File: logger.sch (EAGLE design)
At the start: 131 parts, among them IC1 LTC4412, IC2 ATMEGA8, IC3 FT232RL, IC4 ATMEGA8, IC5 FT232RL, J1 POWER_JACKPTH, Q1 FDN360P, Q2 FDN360P, Q3 16MHz, Q4 16MHz, Q5 2N7002PW, U1 FT232RL, U2 FT232RLSSOP, U3 FT231XS, X5 USB-MICROB

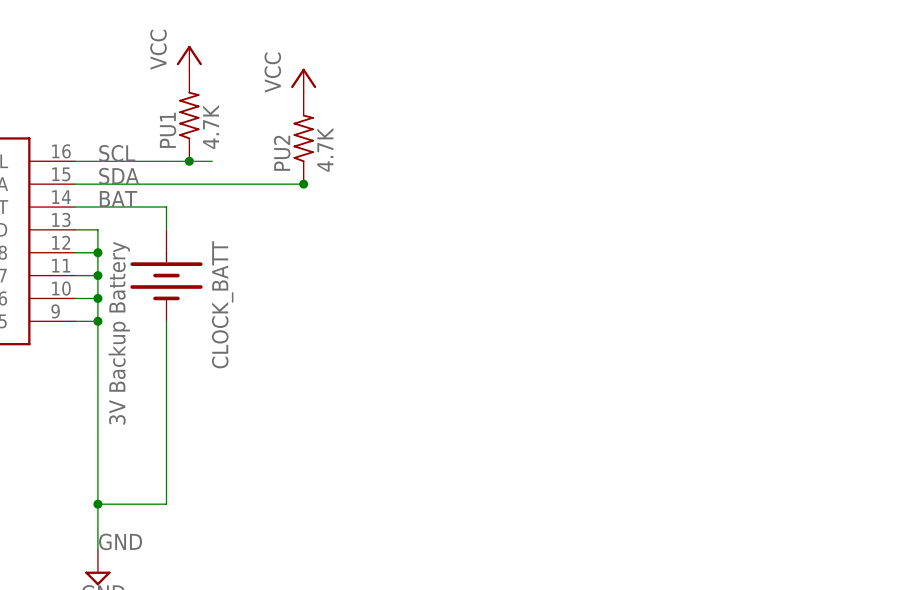
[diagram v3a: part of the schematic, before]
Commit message: Added diode OR, not connected yet
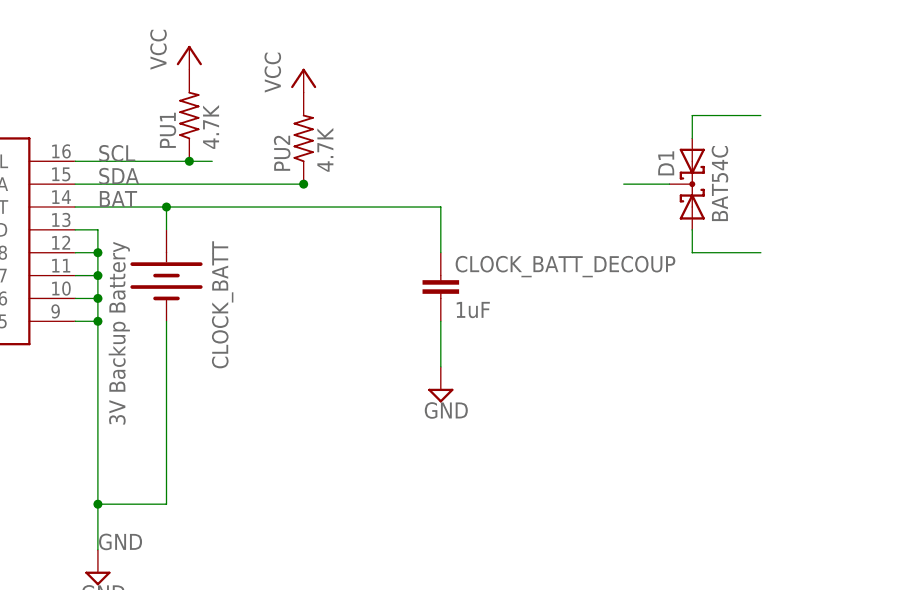
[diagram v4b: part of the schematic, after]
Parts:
- added CLOCK_BATT_DECOUP: 1uF, rcl:C-EUC0603
- added D1: BAT54C, diode:BAT54C
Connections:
- new net N$66: D1.A1
- new net N$67: D1.A2
- new net N$68: D1.CC
- net BAT: now also CLOCK_BATT_DECOUP.1
- net GND: now also CLOCK_BATT_DECOUP.2
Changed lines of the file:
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@@
 <setting verticaltext="up"/>
 </settings>
-<grid distance="0.1" unitdist="inch" unit="inch" style="lines" multiple="1" display="yes" altdistance="0.01" altunitdist="inch" altunit="inch"/>
+<grid distance="0.1" unitdist="inch" unit="inch" style="lines" multiple="1" display="no" altdistance="0.01" altunitdist="inch" altunit="inch"/>
 <layers>
 <layer number="1" name="Top" color="4" fill="1" visible="no" active="no"/>
@@
 <part name="SUPPLY46" library="supply2" deviceset="GND" device=""/>
 <part name="U$9" library="MyPOW" deviceset="VUSB" device=""/>
+<part name="CLOCK_BATT_DECOUP" library="rcl" deviceset="C-EU" device="C0603" value="1uF"/>
+<part name="SUPPLY47" library="supply2" deviceset="GND" device=""/>
+<part name="D1" library="diode" deviceset="BAT54C" device=""/>
 </parts>
 <sheets>
@@
 <instance part="SUPPLY46" gate="GND" x="-91.44" y="-154.94"/>
 <instance part="U$9" gate="G$1" x="17.78" y="-111.76"/>
+<instance part="CLOCK_BATT_DECOUP" gate="G$1" x="312.42" y="208.28"/>
+<instance part="SUPPLY47" gate="GND" x="312.42" y="195.58"/>
+<instance part="D1" gate="G$1" x="340.36" y="218.44" rot="R90"/>
 </instances>
 <busses>
@@
 <pinref part="SUPPLY46" gate="GND" pin="GND"/>
 </segment>
+<segment>
+<pinref part="CLOCK_BATT_DECOUP" gate="G$1" pin="2"/>
+<pinref part="SUPPLY47" gate="GND" pin="GND"/>
+<wire x1="312.42" y1="198.12" x2="312.42" y2="203.2" width="0.1524" layer="91"/>
+</segment>
 </net>
 <net name="TX-O" class="0">
@@
 <pinref part="CLOCK_BATT" gate="G$1" pin="+"/>
 <pinref part="RTC" gate="G$1" pin="VBAT"/>
+<wire x1="281.94" y1="215.9" x2="312.42" y2="215.9" width="0.1524" layer="91"/>
+<junction x="281.94" y="215.9"/>
+<wire x1="312.42" y1="215.9" x2="312.42" y2="210.82" width="0.1524" layer="91"/>
+<pinref part="CLOCK_BATT_DECOUP" gate="G$1" pin="1"/>
 </segment>
 </net>
@@
 </segment>
 </net>
+<net name="N$66" class="0">
+<segment>
+<pinref part="D1" gate="G$1" pin="A1"/>
+<wire x1="340.36" y1="213.36" x2="340.36" y2="210.82" width="0.1524" layer="91"/>
+<wire x1="340.36" y1="210.82" x2="347.98" y2="210.82" width="0.1524" layer="91"/>
+</segment>
+</net>
+<net name="N$67" class="0">
+<segment>
+<pinref part="D1" gate="G$1" pin="A2"/>
+<wire x1="340.36" y1="223.52" x2="340.36" y2="226.06" width="0.1524" layer="91"/>
+<wire x1="340.36" y1="226.06" x2="347.98" y2="226.06" width="0.1524" layer="91"/>
+</segment>
+</net>
+<net name="N$68" class="0">
+<segment>
+<pinref part="D1" gate="G$1" pin="CC"/>
+<wire x1="337.82" y1="218.44" x2="332.74" y2="218.44" width="0.1524" layer="91"/>
+</segment>
+</net>

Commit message: New FTDI chip, power-saving clock circuits (h/t Gerhard), with Chad Sandell
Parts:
- removed C1, C10, C11, C12, C13, C16, C4, C5, C8, C9: 100n, rcl:C-EU
- removed C2, C3, C6, C7: 22p, rcl:C-EU
- removed C_RESET, USBD0, USBD2, USBD4: 0.1uF, resistor:C-EUC0603
- removed F1, F2: 500mA, rcl:L-EUL1812
- removed IC2, IC4: ATMEGA8, atmel:AT90S4433P
- removed IC3, IC5: FT232RL, SmartPrj:FT232RL
- removed J2, J3, J5, J6: (no value), pinhead:PINHD-1X8
- removed J4, J7: (no value), pinhead:PINHD-1X6
- removed JP7, JP8: USB-B, SparkFun-Connectors:USBPTH
- removed Q3, Q4: 16MHz, crystal:CRYTALHC49S
- removed R1, R3, R4, R5, R6, R7, R8, R9: 1k, rcl:R-EU_
- removed R10, R2: 100_NM, rcl:R-EU_
- removed R16: 10k, SparkFun-Passives:RESISTOR0402-RES
- removed RX, TX: (no value), SparkFun-LED:LED0603
- removed RX1, RX2, TX1, TX2: (no value), led:LED0805ROUND
- removed RX_SW: 1Kohm, rcl:R-US_R0603
- removed R_RXLED, R_TXLED, TX_SW: 1K, rcl:R-US_R0603
- removed SJ1: (no value), SparkFun-Passives:SOLDERJUMPER_2WAYS
- removed SJ2: TXLED, SparkFun-Passives:SOLDERJUMPERTRACE
- removed SJ3: RXLED, SparkFun-Passives:SOLDERJUMPERTRACE
- removed U1: FT232RL, SparkFun-DigitalIC:FT232RL-BASICSSOP
- removed U2: FT232RLSSOP, SparkFun-DigitalIC:FT232RLSSOP
- removed USBD1, USBD3, USBD5: 10uF, SparkFun:CAP_POL1206
- removed X1, X3: (no value), jumper:JP4E
- removed X2, X4: (no value), SmartPrj:PN61729
- removed X5: USB-MICROB, SparkFun-Connectors:USB-MICROB
- added PU3, PU4: 3K, rcl:R-US_R0603
- added RCKL1, RCLK2: 220ohm, rcl:R-US_R0603
- added RX_SW1: 1Kohm, rcl:R-US_R0603
- added TX_SW1: 1K, rcl:R-US_R0603
- added U$3, U$4: BSS138, SteveMarple:BSS138SOT23-3-HAND
- PU1, PU2: value 4.7K -> 3K
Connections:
- removed net +5V: C1.1, C10.1, C12.1, C5.1, IC2.AVCC, IC2.VCC, IC3.RESET#, IC3.VCC5I, IC3.VCCIO, IC4.AVCC, IC4.VCC, IC5.RESET#, IC5.VCC5I, IC5.VCCIO, R1.2, R3.2, R4.2, R5.2
- removed net AREF: IC2.AREF, IC4.AREF
- removed net CBUS0: U3.CBUS0
- removed net CBUS3: U3.CBUS3
- removed net CTS: IC3.CTS#, IC5.CTS#, U3.!CTS, X1.1, X3.1
- removed net D+: IC3.USBDP, IC5.USBDP, X2.3, X4.3
- removed net D-: IC3.USBDM, IC5.USBDM, X2.2, X4.2
- removed net M8RXD: IC3.TXD, IC5.TXD, R6.2, R8.2
- removed net M8TXD: IC3.RXD, IC5.RXD, R7.2, R9.2
- removed net MISO: IC2.(MISO)PB4, IC4.(MISO)PB4, J3.5, J6.5
- removed net MOSI: IC2.(MOSI)PB3, IC4.(MOSI)PB3, J3.4, J6.4
- removed net N$10: TX_SW.1, U1.RXD
- removed net N$11: C2.2, IC2.XTAL1, Q3.1
- removed net N$12: C3.2, IC2.XTAL2, Q3.2
- removed net N$13: IC2.(INT0)PD2, J2.3
- removed net N$14: IC2.(INT1)PD3, J2.4
- removed net N$15: IC2.(T0)PD4, J2.5
- removed net N$16: IC2.(T1)PD5, J2.6
- removed net N$17: IC2.(AIN0)PD6, J2.7
- removed net N$18: IC2.(AIN1)PD7, J2.8
- removed net N$19: IC2.(ADC0)PC0), J4.1
- removed net N$20: IC2.(ADC1)PC1, J4.2
- removed net N$21: IC2.(ADC2)PC2, J4.3
- removed net N$22: IC2.(ADC3)PC3, J4.4
- removed net N$23: IC2.(ADC4)PC4, J4.5
- removed net N$24: IC2.(ADC5)PC5, J4.6
- removed net N$25: IC2.(ICP)PB0, J3.1
- removed net N$26: IC2.(OC1)PB1, J3.2
- removed net N$28: F1.2, X4.1
- removed net N$3: JP5.D-, U1.USBDM
- removed net N$30: IC4.(INT0)PD2, J5.3
- removed net N$31: IC4.(INT1)PD3, J5.4
- removed net N$32: IC3.GPIO1, RX1.C
- removed net N$33: IC4.(T0)PD4, J5.5
- removed net N$34: IC3.GPIO0, TX1.C
- removed net N$35: R4.1, RX1.A
- removed net N$36: R5.1, TX1.A
- removed net N$37: IC4.(T1)PD5, J5.6
- removed net N$38: IC4.(AIN0)PD6, J5.7
- removed net N$39: IC4.(AIN1)PD7, J5.8
- removed net N$4: TX.C, U1.TXLED
- removed net N$40: IC4.(ADC0)PC0), J7.1
- removed net N$41: IC4.(ADC1)PC1, J7.2
- removed net N$42: IC4.(ADC2)PC2, J7.3
- removed net N$43: IC4.(ADC3)PC3, J7.4
- removed net N$44: IC4.(ADC4)PC4, J7.5
- removed net N$45: IC4.(ADC5)PC5, J7.6
- removed net N$46: IC4.(ICP)PB0, J6.1
- removed net N$47: IC4.(OC1)PB1, J6.2
- removed net N$48: IC5.GPIO1, RX2.C
- removed net N$49: IC5.GPIO0, TX2.C
- removed net N$5: RX.A, R_RXLED.2
- removed net N$50: R1.1, RX2.A
- removed net N$51: R3.1, TX2.A
- removed net N$52: F2.2, X2.1
- removed net N$53: IC5.AGND, IC5.GND1, IC5.GND2, IC5.GND3, IC5.TEST
- removed net N$54: JP7.D+, U2.USBDP
- removed net N$55: JP7.D-, U2.USBDM
- removed net N$6: R_TXLED.2, TX.A
- removed net N$62: R13.1, SJ2.2
- removed net N$63: R14.1, SJ3.2
- removed net N$64: JP8.D+
- removed net N$65: JP8.D-
- removed net N$66: D1.A1
- removed net N$9: RX_SW.1, U1.TXD
- removed net PD0: IC2.(RXD)PD0, J2.1, R8.1
- removed net PD1: IC2.(TXD)PD1, J2.2, R9.1
- removed net PD2: IC4.(RXD)PD0, J5.1, R6.1
- removed net PD3: IC4.(TXD)PD1, J5.2, R7.1
- removed net RXD: U3.RXD
- removed net SCK: IC2.(SCK)PB5, IC4.(SCK)PB5, J3.6, J6.6
- removed net SS: IC2.(SS)PB2, IC4.(SS)PB2, J3.3, J6.3
- removed net TXD: U3.TXD
- removed net USBVCC: C4.1, C9.1, F1.1, F2.1
- removed net VCC3O: C11.2, C8.2, IC3.VCC30, IC5.VCC30
- removed net VOUT: R16.2, SJ1.2
- new net SCL_3V3: PU4.1, RTC.SCL, U$4.S
- new net SDA_3V3: PU3.1, RTC.SDA, U$3.S
- net 3.3V: now also C20.1, U3.!RESET, U3.3V3OUT, U3.VCCIO; no longer SJ1.1
- net BAT: no longer CLOCK_BATT.+
- net DCD: no longer IC3.DCD#, IC5.DCD#, X1.3, X3.3
- net DSR: no longer IC3.DSR#, IC5.DSR#, X1.2, X3.2
- net DTR: no longer C13.1, C16.1, C_RESET.1, IC3.DTR#, IC5.DTR#, U1.DTR
- net GND: now also U3.!CTS; no longer C1.2, C10.2, C11.1, C12.2, C2.1, C3.1, C4.2, C5.2, C6.1, C7.1, C8.1, C9.2, IC2.AGND, IC2.GND, IC3.AGND, IC3.GND1, IC3.GND2, IC3.GND3, IC3.TEST, IC4.AGND, IC4.GND, JP7.GND, JP8.GND, U1.AGND, U1.CTS, U1.GND1, U1.GND2, U1.GND3, U1.TEST, U2.AGND, U2.GND18, U2.GND21, U2.GND7, U2.TEST, USBD0.2, USBD1.-, USBD2.2, USBD3.-, USBD4.2, USBD5.-, X2.4, X2.P$1, X2.P$2, X4.4, X4.P$1, X4.P$2, X5.GND
- net N$1: now also D1.A1, RCLK2.1; no longer RX.C, U1.RXLED
- net N$2: now also CLOCK_BATT.+, RCLK2.2; no longer JP5.D+, U1.USBDP
- net N$27: now also RX_SW1.1, U3.TXD; no longer C6.2, IC4.XTAL1, Q4.1
- net N$29: now also TX_SW1.1, U3.RXD; no longer C7.2, IC4.XTAL2, Q4.2
- net N$58: now also JP5.D+; no longer X5.D+
- net N$59: now also JP5.D-; no longer X5.D-
- net N$67: now also RCKL1.1
- net RESET: no longer C13.2, C16.2, C_RESET.2, IC2.RESET, IC4.RESET, R10.2, R16.1, R2.2
- net RI: no longer IC3.RI#, IC5.RI#, X1.4, X3.4
- net RTS: no longer IC3.RTS#, IC5.RTS#, R10.1, R2.1
- net RX-I: now also RX_SW1.2; no longer RX_SW.2
- net RXLED: now also R14.1; no longer SJ3.1
- net SCL: now also PU2.1, U$4.D; no longer PU1.1, RTC.SCL
- net SDA: now also PU1.1, U$3.D; no longer PU2.1, RTC.SDA
- net TX-O: now also TX_SW1.2; no longer TX_SW.2
- net TXLED: now also R13.1; no longer SJ2.1
- net VCC: now also RCKL1.2; no longer C17.1, C21.+, RTC.VCC, SJ1.3, X5.VBUS
- net VDD: now also PU3.2, PU4.2, RTC.VCC, U$3.G, U$4.G
- net VUSB: now also C17.1, C21.+; no longer C20.1, JP7.VBUS, JP8.VBUS, R_RXLED.1, R_TXLED.1, U1.VCC, U1.VCCIO, U2.VCC, U2.VCCIO, U3.!RESET, U3.VCCIO, USBD0.1, USBD1.+, USBD2.1, USBD3.+, USBD4.1, USBD5.+
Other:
- note removed: "0"
- note removed: "1"
- note removed: "10"
- note removed: "11"
- note removed: "12"
- note removed: "13"
- note removed: "2"
- note removed: "3"
- note removed: "4"
- note removed: "5"
- note removed: "6"
- note removed: "7"
- note removed: "8"
- note removed: "9"
- note removed: "Arduino 2009"
- moved on the sheet: C17, C18, C19, C20, C21, CLOCK_BATT, CLOCK_BATT_DECOUP, D1, LED1, LED2, PU1, PU2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

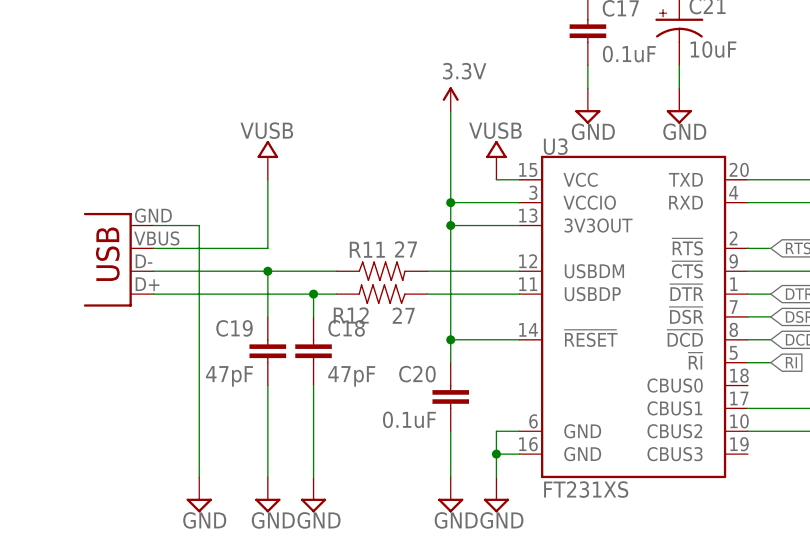
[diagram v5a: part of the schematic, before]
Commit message: routed board with clock power-save and new FTDI
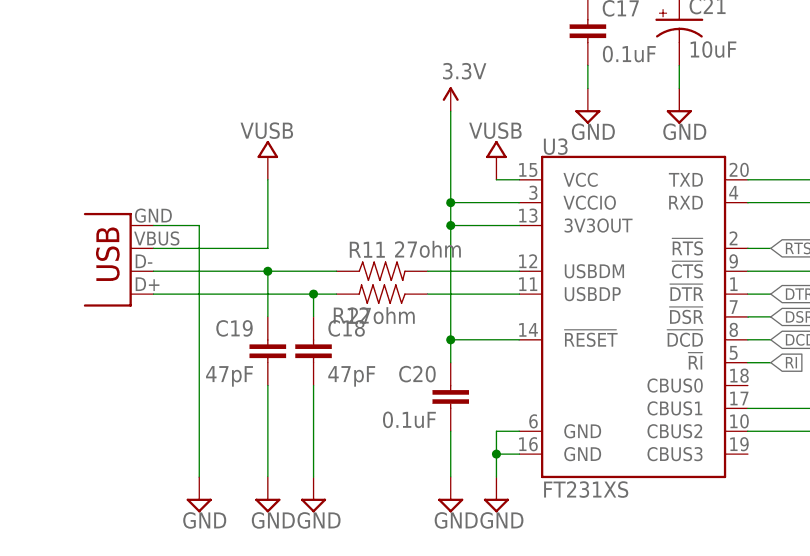
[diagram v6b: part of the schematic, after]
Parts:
- R11, R12: value 27 -> 27ohm
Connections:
- net N$60 renamed TXLED-
- net N$61 renamed RXLED-
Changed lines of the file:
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@@
 <part name="C18" library="SparkFun-Capacitors" deviceset="CAP" device="0402-CAP" value="47pF"/>
 <part name="C19" library="SparkFun-Capacitors" deviceset="CAP" device="0402-CAP" value="47pF"/>
-<part name="R11" library="SparkFun-Resistors" deviceset="RESISTOR" device="0402-RES" value="27"/>
-<part name="R12" library="SparkFun-Resistors" deviceset="RESISTOR" device="0402-RES" value="27"/>
+<part name="R11" library="SparkFun-Resistors" deviceset="RESISTOR" device="0402-RES" value="27ohm"/>
+<part name="R12" library="SparkFun-Resistors" deviceset="RESISTOR" device="0402-RES" value="27ohm"/>
 <part name="C20" library="SparkFun-Capacitors" deviceset="CAP" device="0402-CAP" value="0.1uF"/>
 <part name="C21" library="SparkFun-Passives" deviceset="CAP_POL" device="1206" value="10uF"/>
@@
 </segment>
 </net>
-<net name="N$60" class="0">
+<net name="TXLED-" class="0">
 <segment>
 <pinref part="LED2" gate="G$1" pin="C"/>
@@
 </segment>
 </net>
-<net name="N$61" class="0">
+<net name="RXLED-" class="0">
 <segment>
 <pinref part="LED1" gate="G$1" pin="C"/>
